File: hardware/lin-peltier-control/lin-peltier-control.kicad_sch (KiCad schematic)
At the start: 27 parts, among them J1 UPDI, J2 I2C LCD, J3 LINBus, Q1 2N7002, Q2 2N7002, U1 TJA1021T, U2 ATtiny824-X, U3 PCA9536DP

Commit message: Update the peltier controller to include INA219.
- resistor value to be changed in a bit.
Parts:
- removed JP2: A3, Jumper:SolderJumper-2_P1.3mm_Open_TrianglePad1.0x1.5mm, symbol Jumper:SolderJumper_2_Open
- removed JP3: A2, Jumper:SolderJumper-2_P1.3mm_Open_TrianglePad1.0x1.5mm, symbol Jumper:SolderJumper_2_Open
- removed JP4: A1, Jumper:SolderJumper-2_P1.3mm_Open_TrianglePad1.0x1.5mm, symbol Jumper:SolderJumper_2_Open
- removed JP5: A0, Jumper:SolderJumper-2_P1.3mm_Open_TrianglePad1.0x1.5mm, symbol Jumper:SolderJumper_2_Open
- removed U3: PCA9536DP, Package_SO:TSSOP-8_3x3mm_P0.65mm, symbol Interface_Expansion:PCA9536DP
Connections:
- net SCL3V renamed SCL
- net SDA3V renamed SDA
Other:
- note removed: "I2C Address 0x41"
- moved on the sheet: D2, J1, JP1, R6

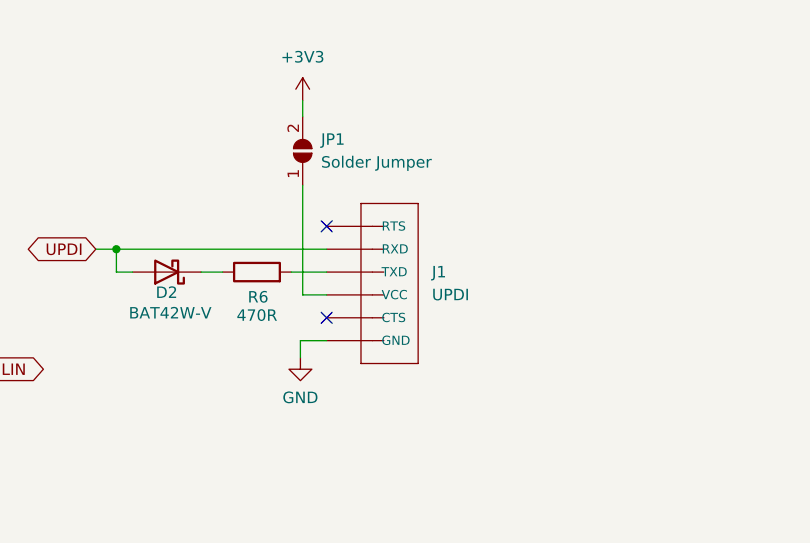
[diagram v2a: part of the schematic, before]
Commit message: Update the schematics... remove PCA9536, use voltage regulator
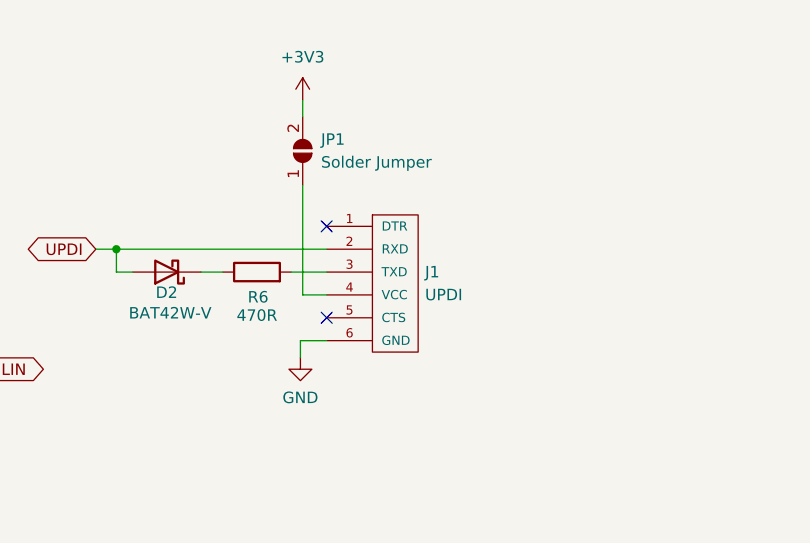
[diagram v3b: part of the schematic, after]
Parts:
- J1: footprint Beirdo:FTDI_BASIC -> Beirdo:FTDI-TARGET; symbol Beirdo:FTDI_BASICPTH -> Beirdo:FTDI-TARGET
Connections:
- net GND: now also J1.6 (GND); no longer J1.1 (GND)
- net UPDI: now also J1.2 (RXD); no longer J1.5 (RXD)
- net at J1.3 (TXD): now also R6.2; no longer JP1.1 (A)
- net at J1.4 (VCC): now also JP1.1 (A); no longer R6.2
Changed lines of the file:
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@@
     (pin "2")
   )
-  (symbol (lib_id "Beirdo:FTDI_BASICPTH") (at 161.798 163.195 0) (mirror y) (unit 1)
-    (in_bom yes) (on_board yes) (fields_autoplaced)
-    (property "Reference" "J1" (id 0) (at 168.402 160.6549 0)
-      (effects (font (size 1.27 1.27)) (justify right))
-    )
-    (property "Value" "UPDI" (id 1) (at 168.402 163.1949 0)
-      (effects (font (size 1.27 1.27)) (justify right))
-    )
-    (property "Footprint" "Beirdo:FTDI_BASIC" (id 2) (at 161.036 159.385 0)
+  (symbol (lib_id "Beirdo:FTDI-TARGET") (at 164.338 154.305 0) (unit 1)
+    (in_bom yes) (on_board yes) (fields_autoplaced)
+    (property "Reference" "J1" (id 0) (at 167.64 160.6549 0)
+      (effects (font (size 1.27 1.27)) (justify left))
+    )
+    (property "Value" "UPDI" (id 1) (at 167.64 163.1949 0)
+      (effects (font (size 1.27 1.27)) (justify left))
+    )
+    (property "Footprint" "Beirdo:FTDI-TARGET" (id 2) (at 164.338 173.355 0)
       (effects (font (size 0.508 0.508)) hide)
     )
@@
     )
     (path "/167c96c2-87e0-4fa7-90fa-e306cc431639"
-      (reference "J1") (unit 1) (value "UPDI") (footprint "Beirdo:FTDI_BASIC")
+      (reference "J1") (unit 1) (value "UPDI") (footprint "Beirdo:FTDI-TARGET")
     )
     (path "/896d75c9-afdd-4f00-acd3-b7de4e8fa8a8"
